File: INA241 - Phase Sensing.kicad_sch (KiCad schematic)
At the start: 36 parts, among them IC2 INA241A2IDGKR, IC4 INA241A2IDGKR, IC6 INA241A2IDGKR

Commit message: Fill template pages: block diagram, power sequencing, cover notes, architecture
- Block Diagram redrawn from the real design: phase path (MR60PW, shunts),
  current and voltage channels with their gains and bandwidths, AD7606C-18,
  power chain, target specifications
- Power - Sequencing: start-up curves taken from the LTspice simulations
  (boost soft-start, analog rails) and rail table with sources, levels
  and timings
- Cover page: real design notes instead of the template examples
- Project Architecture: power-supply block documented, contiguous page
  numbers (Power Supply is page 6)
- Revision History: one column fed by the [Unreleased] changelog section
- sheet titles shortened so they fit the cover-page index: INA241 - Phase
  Sensing, Power Supply - Analog Rails

Sheet-level polylines carry no fill attribute (KiBot schematic reader).

Co-Authored-By: Claude Opus 5.5 <noreply@anthropic.com>
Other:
- title: INA241 - Phase Current and Voltage Sense -> INA241 - Phase Sensing
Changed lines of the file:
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@@
 	(paper "A3")
 	(title_block
-		(title "INA241 - Phase Current and Voltage Sense")
+		(title "INA241 - Phase Sensing")
 		(date "2026-10-05")
 		(rev "${REVISION}")

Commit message: Rename the project to OPEN_PHASE
PhaseSense-8586 was named after the first parts of the design (INA240 +
ADS8586S), which are no longer on the board. OPEN_PHASE follows
OPEN_WEIGHT, the other OPEN THRUST LAB board.

- project files: OPEN_PHASE.kicad_pro / _sch / _pcb / _prl / _dru
- libraries: lib/lib_sym/OPEN_PHASE.kicad_sym and
  lib/lib_fp/OPEN_PHASE.pretty, nickname OPEN_PHASE in both tables, in
  every lib_id and in every footprint of the PCB
- project name of every symbol and sheet instance, so the reference
  designators are kept
- PROJECT_NAME and GIT_URL in the project and in kibot_main.yaml, README
  and its template, CHANGELOG, LTspice headers and their generator
- the README note now says the project was first published as
  PhaseSense-8586

The GitHub repository is now foukouda/OPEN_PHASE. The board name
PHASETRACKER is unchanged. The netlist, ERC and DRC reports are the same
before and after the rename.

Co-Authored-By: Claude Opus 5.5 <noreply@anthropic.com>
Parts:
- C1, C10, C17, C18, C2, C25, C29, C31, C32, C33, C34, C5: footprint PhaseSense-8586:C_0603_1608Metric -> OPEN_PHASE:C_0603_1608Metric; symbol PhaseSense-8586:C -> OPEN_PHASE:C
- IC2, IC4, IC6: footprint PhaseSense-8586:SOP65P490X110-8N -> OPEN_PHASE:SOP65P490X110-8N; symbol PhaseSense-8586:INA241A2IDGKR -> OPEN_PHASE:INA241A2IDGKR
- R1, R4, R7: footprint PhaseSense-8586:PBVR001F110 -> OPEN_PHASE:PBVR001F110; symbol PhaseSense-8586:PBV-R001-F1-1.0 -> OPEN_PHASE:PBV-R001-F1-1.0
- R13, R15, R16, R17, R18, R19, R20, R21, R22, Re1, Re2, Re3: footprint PhaseSense-8586:R_0603_1608Metric -> OPEN_PHASE:R_0603_1608Metric; symbol PhaseSense-8586:R -> OPEN_PHASE:R
- R27, R28, R31, R32, R35, R36: footprint PhaseSense-8586:R_0805_2012Metric -> OPEN_PHASE:R_0805_2012Metric; symbol PhaseSense-8586:R -> OPEN_PHASE:R

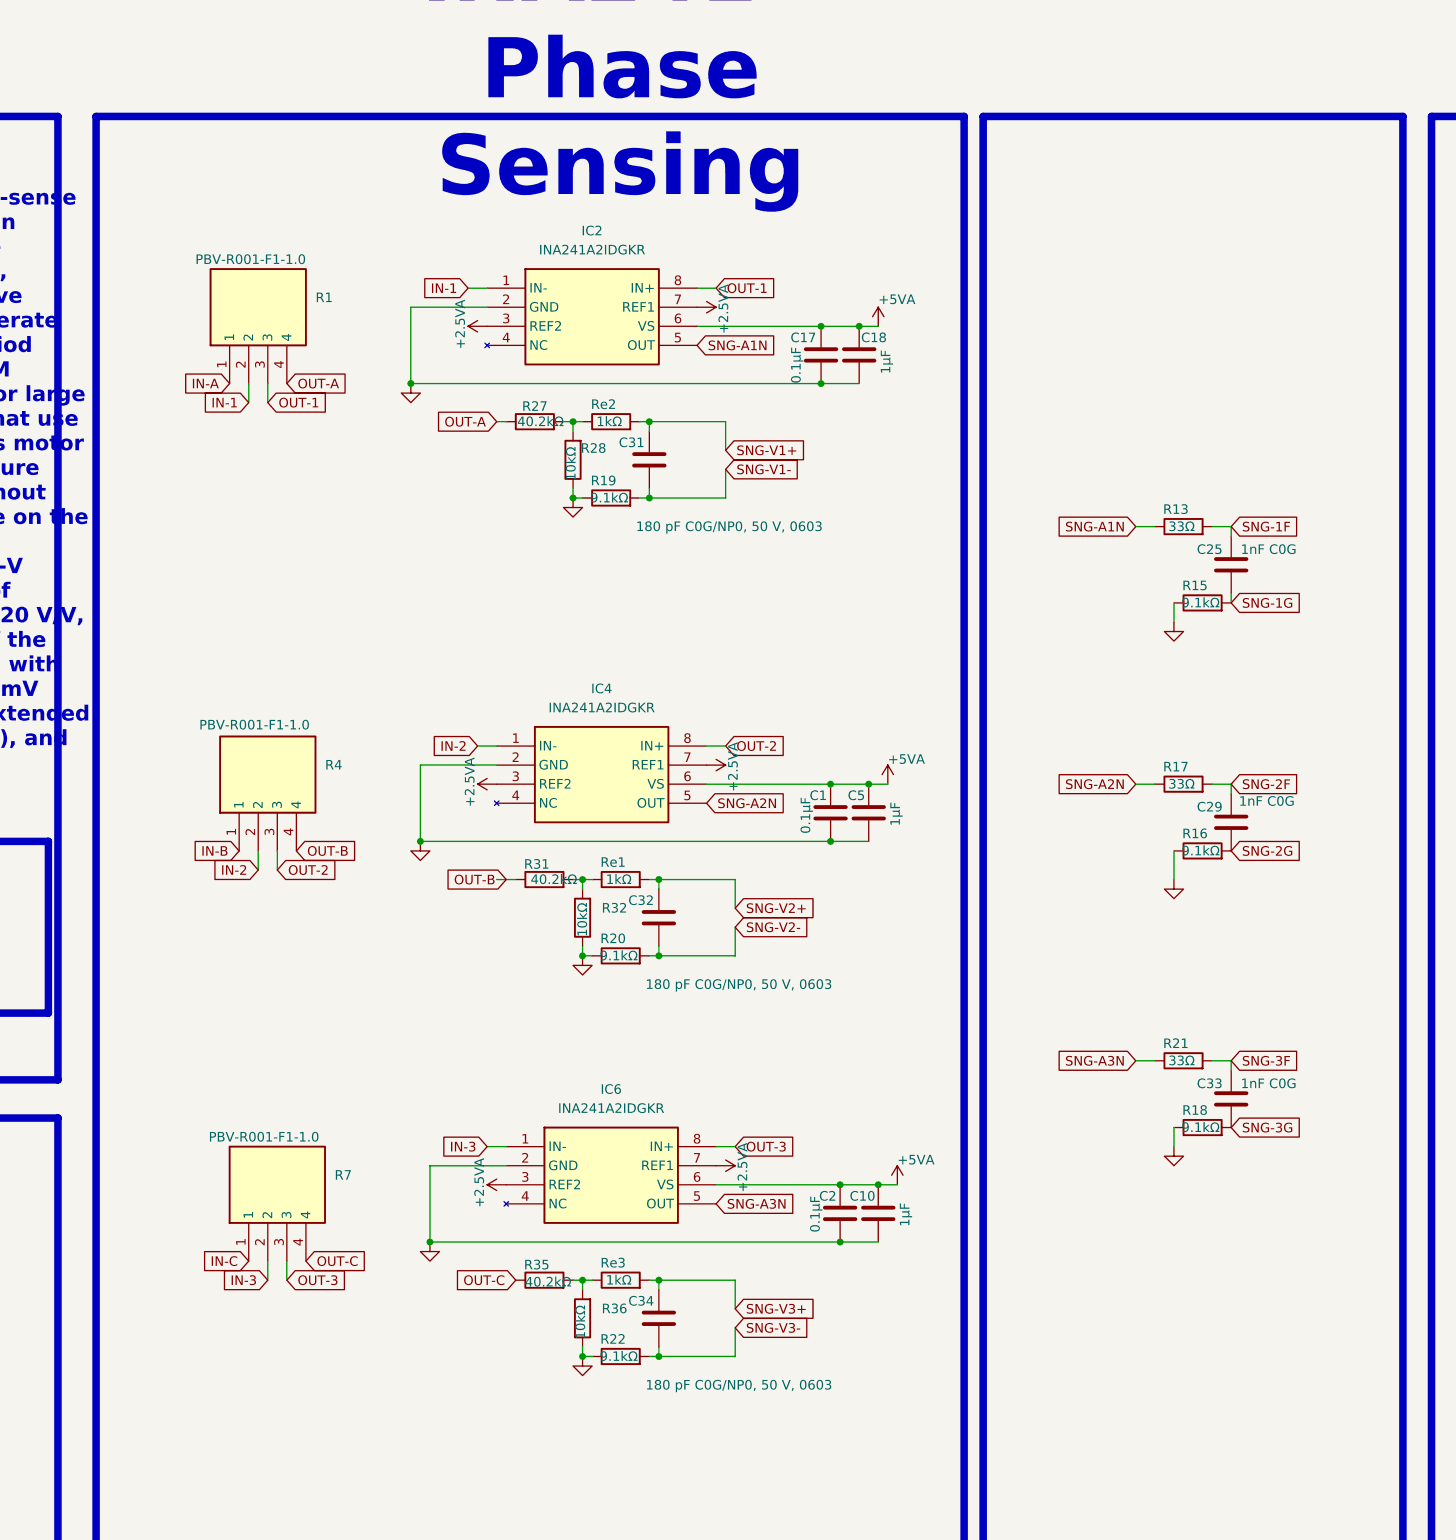
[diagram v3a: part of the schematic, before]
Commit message: Smaller boost inductor, white board, openEMS and thermal simulations
- L1: Wurth 744373965022 (13.5 x 12.5 mm) -> WE-MAPI 4030 74438357022
  (2.2 uH, 4.1 x 4.1 x 3.1 mm, Isat 4.6 A at -10 %, above the 3.1 A LT8362
  switch limit). Footprint and STEP from the KiCad library, copied to lib/.
- Board: solder mask white (custom opaque #F4F4F0F5, the KiCad "White"
  preset renders pink over copper), silkscreen black. kibot_globals.yaml
  names the colours so the fabrication notes print WHITE / BLACK.
- Simulation/openEMS: inductance of the PBV shunts seen by the INA241
  inputs on the routed copper (results.md, figures in Images/Simulation).
- Simulation/Thermal: current density and temperature of the power paths.
- LTspice simulations, figures and README updated; sim07 DC bus figure.
- 3D animation (Images/OPEN_PHASE.mp4, OPEN_PHASE-spin.gif) on the white board.
- XT60PW-F footprint and model, bottom silkscreen cartouches.

Co-Authored-By: Claude Opus 5.5 <noreply@anthropic.com>
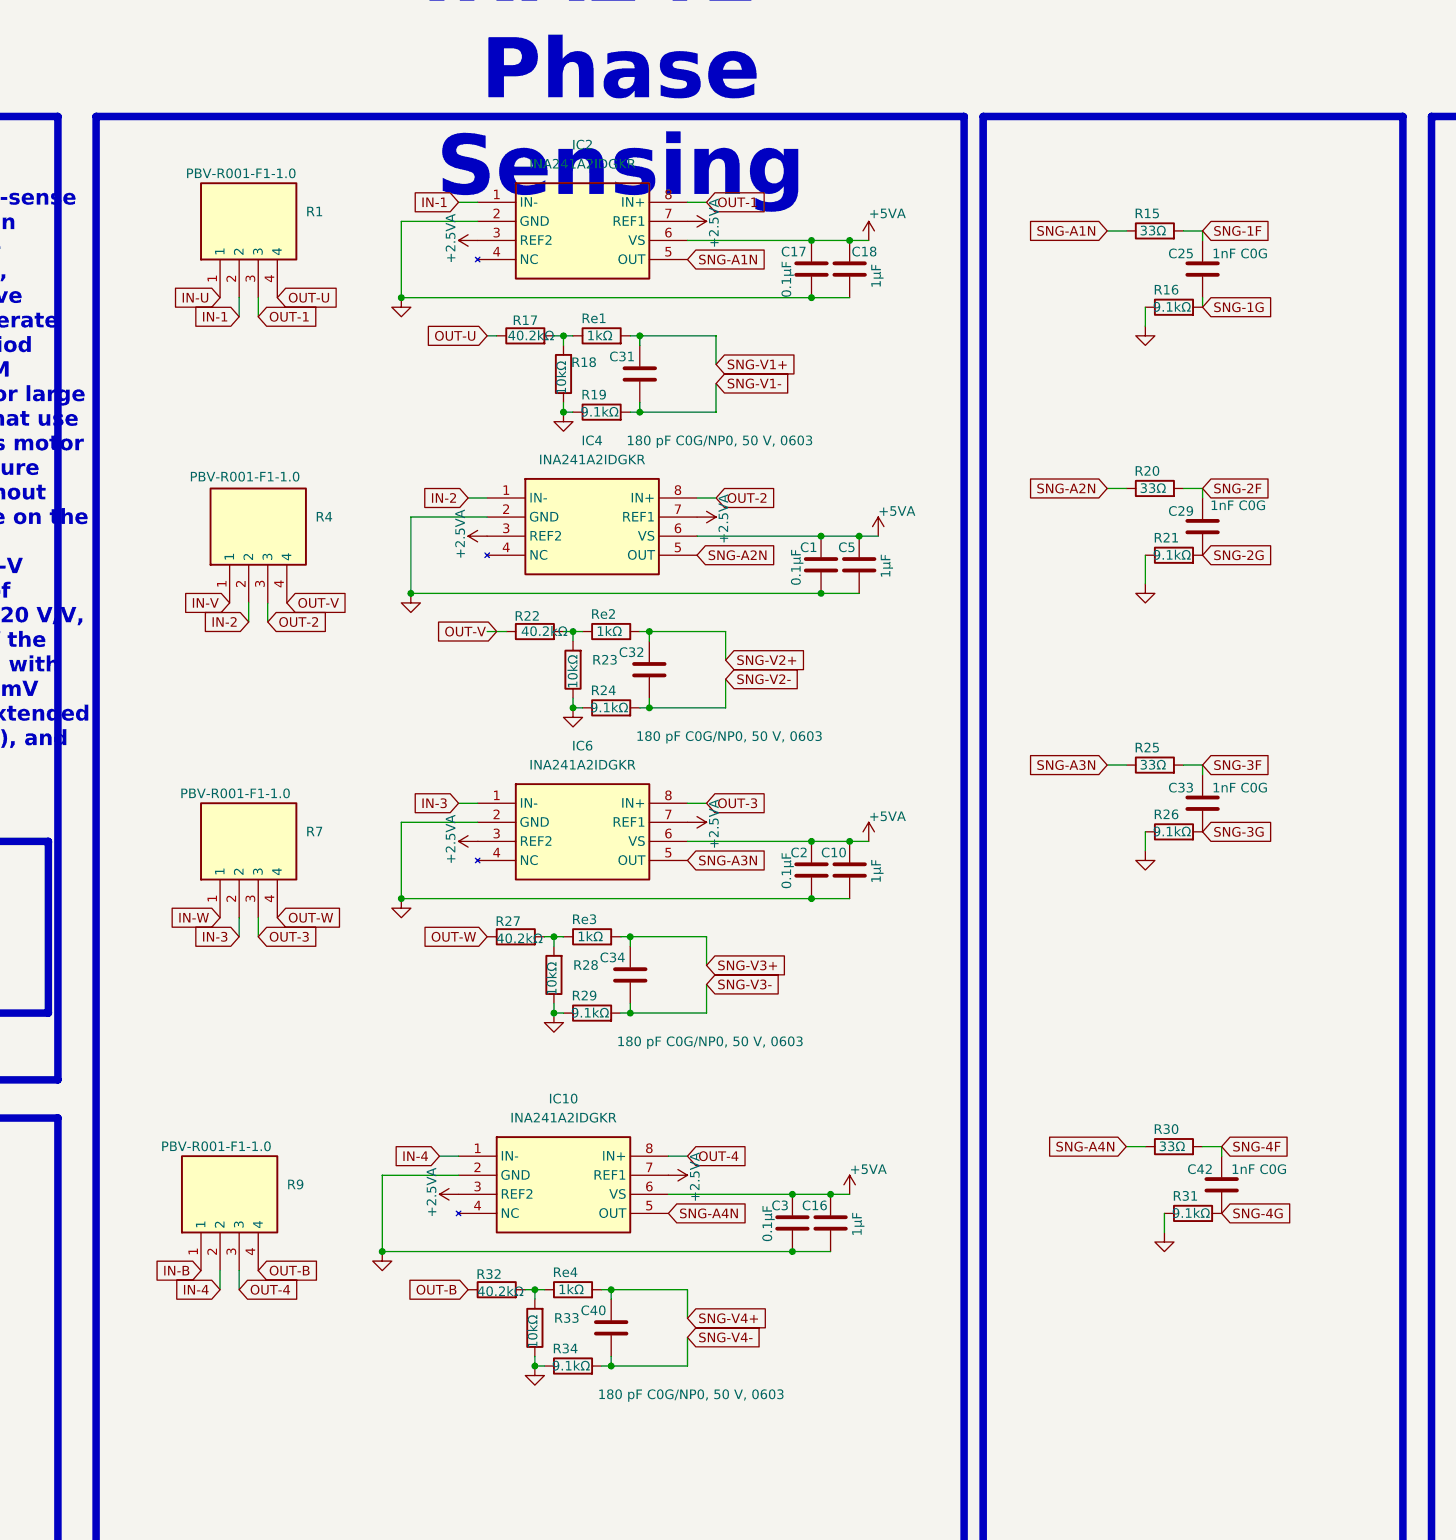
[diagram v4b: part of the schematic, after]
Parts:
- added C16: 1µF, OPEN_PHASE:C_0603_1608Metric, symbol OPEN_PHASE:C
- added C3: 0.1µF, OPEN_PHASE:C_0603_1608Metric, symbol OPEN_PHASE:C
- added C40: 180 pF C0G/NP0, 50 V, 0603, OPEN_PHASE:C_0603_1608Metric, symbol OPEN_PHASE:C
- added C42: 1nF C0G, OPEN_PHASE:C_0603_1608Metric, symbol OPEN_PHASE:C
- added IC10: INA241A2IDGKR, OPEN_PHASE:SOP65P490X110-8N, symbol OPEN_PHASE:INA241A2IDGKR
- added R30: 33Ω, OPEN_PHASE:R_0603_1608Metric, symbol OPEN_PHASE:R
- added R31, R34: 9.1kΩ, OPEN_PHASE:R_0603_1608Metric, symbol OPEN_PHASE:R
- added R32: 40.2kΩ, OPEN_PHASE:R_0805_2012Metric, symbol OPEN_PHASE:R
- added R33: 10kΩ, OPEN_PHASE:R_0805_2012Metric, symbol OPEN_PHASE:R
- added R9: PBV-R001-F1-1.0, OPEN_PHASE:PBVR001F110, symbol OPEN_PHASE:PBV-R001-F1-1.0
- added Re4: 1kΩ, OPEN_PHASE:R_0603_1608Metric, symbol OPEN_PHASE:R
- renumbered R13 to R15, R15 to R16, R27 to R17, R28 to R18, R17 to R20, R16 to R21, R31 to R22, R32 to R23, R20 to R24, R21 to R25, R18 to R26, R35 to R27, R36 to R28, R22 to R29, Re2 to Re1, Re1 to Re2
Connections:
- net +2.5VA: now also IC10.3 (REF2), IC10.7 (REF1)
- net +5VA: now also C16.1, C3.1, IC10.6 (VS)
- net GND: now also C16.2, C3.2, IC10.2 (GND), R31.1, R33.1, R34.1
- net IN-B: now also R9.1; no longer R4.1
- net OUT-B: now also R32.1, R9.4; no longer R22.1, R4.4
- net IN-A renamed IN-U
- net IN-C renamed IN-W
- net OUT-A renamed OUT-U
- net OUT-C renamed OUT-W
- new net: R32.2, R33.2, Re4.1
- new net IN-4: IC10.1 (IN-), R9.2
- new net IN-V: R4.1
- new net OUT-4: IC10.8 (IN+), R9.3
- new net OUT-V: R22.1, R4.4
- new net SNG-4F: C42.1, R30.2
- new net SNG-4G: C42.2, R31.2
- new net SNG-A4N: IC10.5 (OUT), R30.1
- new net SNG-V4+: C40.1, Re4.2
- new net SNG-V4-: C40.2, R34.2
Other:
- moved on the sheet: C1, C10, C17, C18, C2, C25, C29, C31, C32, C33, C34, C5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
